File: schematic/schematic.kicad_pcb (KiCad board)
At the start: 2 copper layers, 70 parts, among them J1 Conn_01x04_Socket, J10 Conn_01x06_Pin, J11 Conn_01x06_Pin, J2 Conn_01x04_Socket, J3 Conn_01x04_Socket, J4 Conn_01x04_Socket, J5 Conn_01x03_Pin, J6 Conn_01x03_Pin, J7 Conn_01x03_Pin, J8 Conn_01x03_Pin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

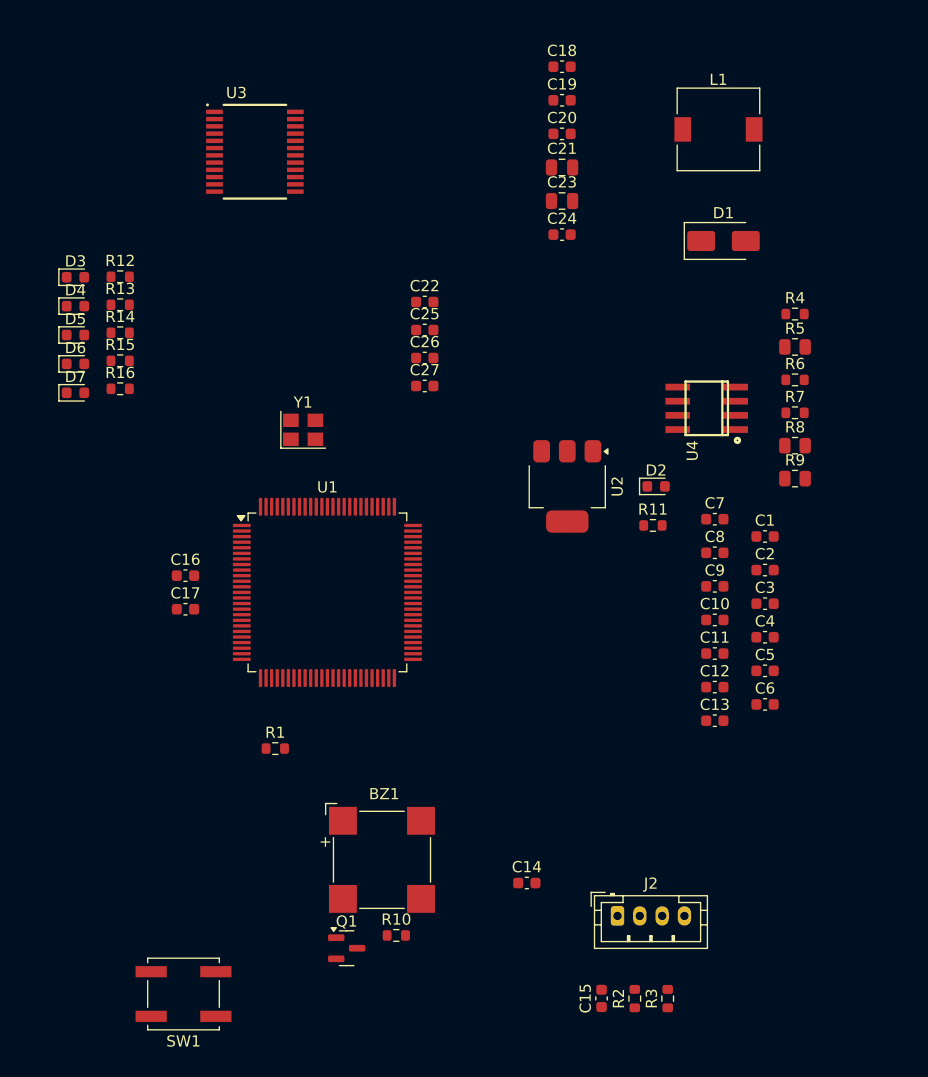
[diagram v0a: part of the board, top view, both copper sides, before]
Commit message: thếu nút nhấn
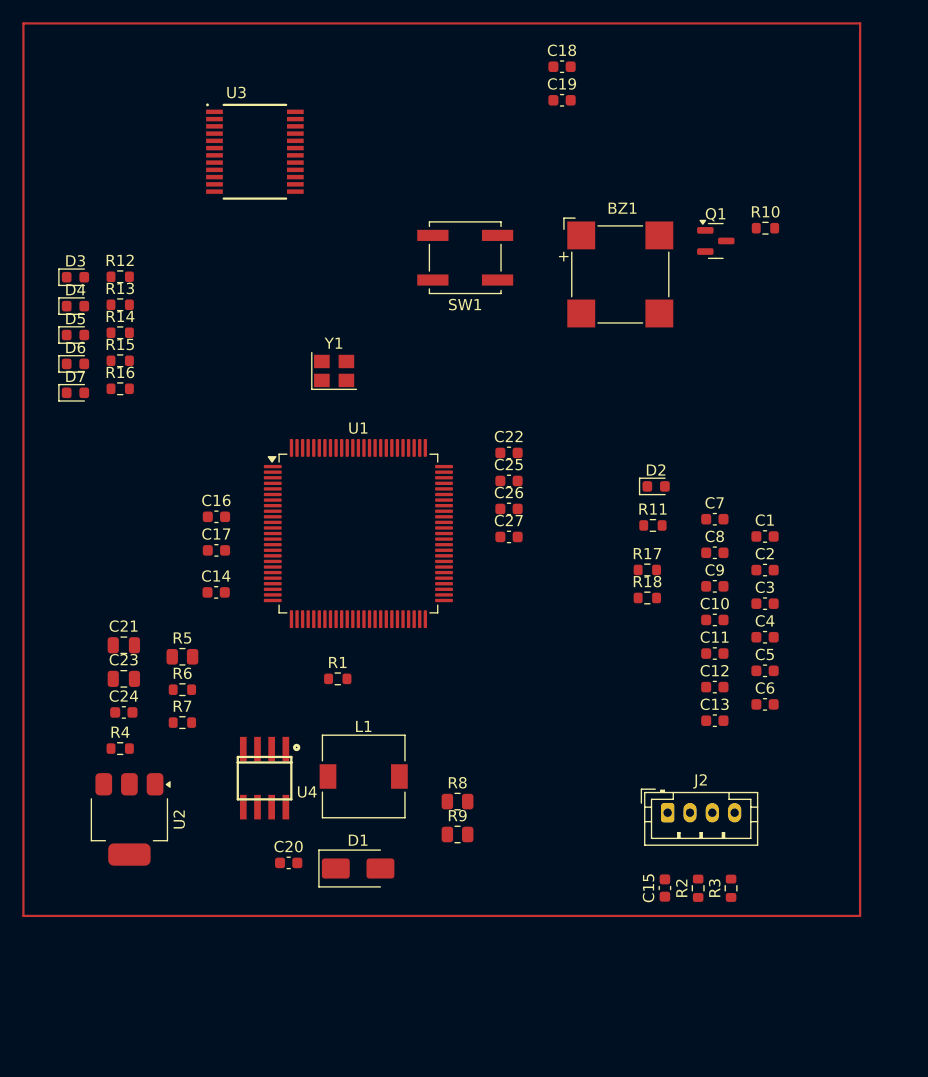
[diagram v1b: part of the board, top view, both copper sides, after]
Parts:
- added R17: 1k, Resistor_SMD:R_0603_1608Metric, F.Cu at (170.7, 97.0)
- added R18: 1k, Resistor_SMD:R_0603_1608Metric, F.Cu at (170.7, 99.5)
- moved R4 71.9 mm to (123.4, 113.0)
- moved Q1 71.5 mm to (176.8, 67.5)
- moved R10 71.5 mm to (181.3, 66.4)
- moved SW1 70.7 mm to (154.3, 69.0)
- moved C20 69.8 mm to (138.5, 123.2)
- moved L1 66.1 mm to (145.2, 115.5)
- moved D1 65.1 mm to (144.8, 123.8)
- moved R5 61.5 mm to (129.0, 104.8)
- moved R6 61.5 mm to (129.0, 107.7)
- moved R7 61.5 mm to (129.0, 110.7)
- moved C21 58.1 mm to (123.8, 103.7)
- moved C23 58.1 mm to (123.8, 106.8)
- moved C24 58.1 mm to (123.8, 109.8)
- moved BZ1 56.7 mm to (168.2, 70.5)
- moved U4 51.7 mm to (136.4, 115.7), turned to 180 degrees
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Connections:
- net /Encoder_A_L renamed /EN_A_L
- net /Encoder_A_R renamed /EN_A_R
- net /Encoder_B_L renamed /EN_B_L
- net /Encoder_B_R renamed /EN_B_R
- net /sensorFF renamed /SS_FF
- net /sensorFL renamed /SS_FL
- net /sensorFR renamed /SS_FR
- net /sensorL renamed /SS_L
- net /sensorR renamed /SS_R

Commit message: no message
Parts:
- added C28: 100nF, Capacitor_SMD:C_0603_1608Metric, F.Cu at (136.2, 86.7)
- added C29: 100nF, Capacitor_SMD:C_0603_1608Metric, F.Cu at (136.2, 89.2)
- added R19: 1k, Resistor_SMD:R_0603_1608Metric, F.Cu at (144.2, 84.1)
- added R20: 1k, Resistor_SMD:R_0603_1608Metric, F.Cu at (144.2, 86.7)
- added SW2: SW_Push, Button_Switch_SMD:SW_Tactile_SPST_NO_Straight_CK_PTS636Sx25SMTRLFS, F.Cu at (151.5, 75.7)
- added SW3: SW_Push, Button_Switch_SMD:SW_Tactile_SPST_NO_Straight_CK_PTS636Sx25SMTRLFS, F.Cu at (151.5, 81.0)
- C12, C13, C26, C27: moved to B.Cu
- R17, R18: value 1k -> 4.7k
- SW1: footprint Button_Switch_SMD:SW_Push_1P1T_NO_CK_KSC6xxJ -> Button_Switch_SMD:SW_Tactile_SPST_NO_Straight_CK_PTS636Sx25SMTRLFS
- moved C19 129.5 mm to (54.3, 125.2), turned to 180 degrees
- moved C13 122.4 mm to (57.4, 83.3), turned to 180 degrees
- moved J7 119.7 mm to (107.2, 89.5)
- moved C12 119.6 mm to (57.9, 93.5), turned to 90 degrees
- moved C4 114.8 mm to (69.0, 78.9)
- moved C18 114.7 mm to (62.5, 107.0), turned to 90 degrees
- moved C6 113.3 mm to (69.0, 93.3)
- moved C5 112.5 mm to (69.1, 97.6)
- moved C2 112.3 mm to (69.0, 91.3)
- moved C1 112.2 mm to (69.0, 95.6)
- moved C3 112.2 mm to (69.1, 99.3)
- moved J6 107.8 mm to (107.2, 79.8)
- moved J1 106.0 mm to (117.2, 70.5)
- moved C11 105.8 mm to (73.2, 82.8)
- moved C10 105.6 mm to (73.2, 80.7)
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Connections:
- U1 pad 82: unconnected-(U1-PD1-Pad82) -> /BUTTON_0
- U1 pad 83: unconnected-(U1-PD2-Pad83) -> /BUTTON_1
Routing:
- net +5V: track 0.00 -> 35.2 mm, vias 0 -> 2
- net +3V3: track 0.00 -> 14.2 mm
- net Net-(U4-FREQ): track 0.00 -> 14.1 mm
- net Net-(U4-BST): track 0.00 -> 13.0 mm, vias 0 -> 2
- net Net-(U4-EN): track 0.00 -> 10.7 mm
- net Net-(U4-FB): track 0.00 -> 7.97 mm
- net Net-(D1-K): track 0.00 -> 6.63 mm
- net Net-(U4-COMP): track 0.00 -> 5.29 mm
- net Net-(C13-Pad1): track 0.00 -> 2.49 mm, vias 0 -> 1
- net Net-(U1-BOOT0): track 0.00 -> 2.12 mm
- net Net-(C12-Pad1): track 0.00 -> 2.12 mm, vias 0 -> 1
- net Net-(C21-Pad2): track 0.00 -> 1.83 mm
- net GND: track 0.00 -> 1.40 mm, vias 0 -> 1
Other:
- board outline added: 65 x 85 mm

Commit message: trc khi xoá ve lai
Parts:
- added J12: Conn_01x02_Socket, Connector_JST:JST_XA_B02B-XASK-1_1x02_P2.50mm_Vertical, F.Cu at (158.7, 134.4)
- C1, C10, C11, C14, C16, C17, C18, C2, C3, C4, C5, C6, C7, C8, C9, J10, J11, J5, J6, R19, R20, Y1: moved to B.Cu
- moved D1 119.0 mm to (165.7, 129.8), turned to 0 degrees
- moved C20 115.4 mm to (159.9, 122.8)
- moved R6 112.4 mm to (154.7, 128.0), turned to 180 degrees
- moved L1 111.0 mm to (165.2, 123.1), turned to 90 degrees
- moved C12 102.5 mm to (160.2, 86.2), turned to -90 degrees
- moved U4 101.6 mm to (156.3, 123.1), turned to 180 degrees
- moved U1 101.5 mm to (154.3, 88.9), turned to 90 degrees
- moved C18 101.3 mm to (162.8, 121.3), turned to -90 degrees
- moved C22 98.3 mm to (162.9, 104.8), turned to -90 degrees
- moved C19 98.1 mm to (152.1, 132.2), turned to 90 degrees
- moved C25 96.9 mm to (161.2, 104.8)
- moved R8 96.1 mm to (150.1, 132.4), turned to -90 degrees
- moved R1 95.0 mm to (144.6, 92.9), turned to 90 degrees
- moved C13 94.0 mm to (151.3, 84.4), turned to -90 degrees
- moved R4 92.9 mm to (152.6, 123.0), turned to 90 degrees
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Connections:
- J10 pad 3: /EN_A_R -> /EN_B_L
- J10 pad 4: /EN_B_R -> /EN_A_L
- J10 pad 5: /M1-L -> /M1-R
- J10 pad 6: /M1-R -> /M1-L
- J11 pad 3: /EN_B_L -> /EN_A_R
- J11 pad 4: /EN_A_L -> /EN_B_R
- J4 pad 1: 5V -> +5V
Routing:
- net +3V3: track 14.2 -> 207.7 mm, vias 0 -> 17
- net +5V: track 35.2 -> 115.3 mm, vias 2 -> 13
- net GND: track 1.40 -> 75.5 mm, vias 1 -> 7
- net /EN_A_L: track 0.00 -> 72.9 mm, vias 0 -> 4
- net /PWMA: track 0.00 -> 36.7 mm, vias 0 -> 2
- net /M1-L: track 0.00 -> 33.4 mm
- net /BIN2: track 0.00 -> 32.9 mm, vias 0 -> 2
- net /NRST: track 0.00 -> 31.4 mm, vias 0 -> 3
- net /BIN1: track 0.00 -> 30.7 mm, vias 0 -> 2
- net /M2-L: track 0.00 -> 30.5 mm, vias 0 -> 4
- net /EN_B_L: track 0.00 -> 27.1 mm
- net 6.5-7.5V: track 0.00 -> 24.2 mm
- net /M1-R: track 0.00 -> 24.0 mm
- net /M2-R: track 0.00 -> 23.9 mm, vias 0 -> 4
- net /AIN1: track 0.00 -> 20.8 mm, vias 0 -> 2
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- added copper zone on F.Cu, net +5V
- added copper zone on B.Cu, net GND
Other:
- outline, holes or cut-outs redrawn

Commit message: 1
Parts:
- added C30: 22uF, Capacitor_SMD:C_0201_0603Metric, F.Cu at (84.3, 147.6)
- added C31: 22uF, Capacitor_SMD:C_0201_0603Metric, F.Cu at (84.3, 149.4)
- added R21: 1.1R, Resistor_SMD:R_0805_2012Metric, F.Cu at (80.9, 148.2)
- added RN1: R_Network05, Resistor_SMD:R_Array_Convex_5x0603, F.Cu at (74.2, 130.3)
- added RN2: R_Pack05, Resistor_SMD:R_Array_Convex_5x0603, F.Cu at (51.5, 140.0)
- added SW4: SW_DIP_x05, Button_Switch_SMD:SW_DIP_SPSTx05_Slide_KingTek_DSHP05TS_W7.62mm_P1.27mm, F.Cu at (59.4, 140.2)
- added U5: AMS1117-5.0, Package_TO_SOT_SMD:SOT-223-3_TabPin2, F.Cu at (83.6, 142.6)
- C14, C16, C17, C18, C26, C27, R19, R20, Y1: moved to F.Cu
- J1, J4: footprint Connector_JST:JST_PH_B4B-PH-K_1x04_P2.00mm_Vertical -> Connector_PinHeader_2.54mm:PinHeader_1x04_P2.54mm_Vertical
- J10, J11: footprint Connector_JST:JST_PH_S6B-PH-K_1x06_P2.00mm_Horizontal -> JST-254:JST 6
- J2: footprint Connector_JST:JST_PH_B4B-PH-K_1x04_P2.00mm_Vertical -> Connector_JST:JST_SH_BM04B-SRSS-TB_1x04-1MP_P1.00mm_Vertical
- J5, J6: footprint Connector_JST:JST_PH_S3B-PH-K_1x03_P2.00mm_Horizontal -> Connector_PinHeader_2.54mm:PinHeader_1x03_P2.54mm_Vertical; moved to F.Cu
- J7: footprint Connector_JST:JST_PH_S3B-PH-K_1x03_P2.00mm_Horizontal -> Connector_PinHeader_2.54mm:PinHeader_1x03_P2.54mm_Vertical
- J8, J9: footprint Connector_JST:JST_PH_B3B-PH-K_1x03_P2.00mm_Vertical -> Connector_PinHeader_2.54mm:PinHeader_1x03_P2.54mm_Vertical
- R1, R2, R3: moved to B.Cu
- moved C24 130.0 mm to (57.0, 83.1), turned to 0 degrees
- moved J4 125.5 mm to (49.9, 119.3)
- moved R18 120.4 mm to (65.0, 88.1), turned to 0 degrees
- moved J12 120.4 mm to (40.5, 111.3), turned to 0 degrees
- moved R17 119.3 mm to (65.0, 85.6), turned to 0 degrees
- moved R11 117.7 mm to (61.0, 93.1), turned to 0 degrees
- moved C28 116.9 mm to (57.0, 93.1)
- moved C29 116.9 mm to (57.0, 95.6)
- moved U4 115.6 mm to (40.7, 119.7), turned to 0 degrees
- moved U2 113.8 mm to (63.8, 119.6), turned to 0 degrees
- moved C18 112.7 mm to (53.0, 95.6), turned to 0 degrees
- moved C20 112.2 mm to (57.0, 78.1), turned to 0 degrees
- moved C19 110.7 mm to (57.0, 75.6), turned to 0 degrees
- moved C22 108.7 mm to (57.0, 80.6), turned to 0 degrees
- moved C23 107.4 mm to (69.2, 94.6), turned to 0 degrees
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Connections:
- D3 pad 1: GND -> Net-(D3-K)
- D3 pad 2: Net-(D3-A) -> /LED_FL
- D4 pad 1: GND -> Net-(D4-K)
- D4 pad 2: Net-(D4-A) -> /LED_L
- D5 pad 1: GND -> Net-(D5-K)
- D5 pad 2: Net-(D5-A) -> /LED_FF
- D6 pad 1: GND -> Net-(D6-K)
- D6 pad 2: Net-(D6-A) -> /LED_FR
- D7 pad 1: GND -> Net-(D7-K)
- D7 pad 2: Net-(D7-A) -> /LED_R
- J10 pad 5: /M1-R -> /M2-L
- J10 pad 6: /M1-L -> /M2-R
- J11 pad 5: /M2-L -> /M1-R
- J11 pad 6: /M2-R -> /M1-L
- U1 pad 1: unconnected-(U1-PE2-Pad1) -> /BIT_SW_4
- U1 pad 2: unconnected-(U1-PE3-Pad2) -> /BIT_SW_3
- U1 pad 24: unconnected-(U1-PA2-Pad24) -> /BUTTON_0
- U1 pad 25: unconnected-(U1-PA3-Pad25) -> /BUTTON_1
- U1 pad 29: /EN_A_L -> unconnected-(U1-PA5-Pad29)
- U1 pad 3: unconnected-(U1-PE4-Pad3) -> /BIT_SW_2
- U1 pad 39: /PWMA -> unconnected-(U1-PE9-Pad39)
- U1 pad 4: unconnected-(U1-PE5-Pad4) -> /BIT_SW_1
- U1 pad 41: /PWMB -> unconnected-(U1-PE11-Pad41)
- U1 pad 5: unconnected-(U1-PE6-Pad5) -> /BIT_SW_0
- U1 pad 53: /UART1_TX -> unconnected-(U1-PB14-Pad53)
- U1 pad 54: /UART1_RX -> unconnected-(U1-PB15-Pad54)
- U1 pad 61: unconnected-(U1-PD14-Pad61) -> /BUZZ
- U1 pad 62: unconnected-(U1-PD15-Pad62) -> /LED_L
- U1 pad 63: /LED_L -> /LED_FL
- U1 pad 64: /LED_R -> /LED_FF
- U1 pad 65: /LED_FL -> /LED_FR
- U1 pad 66: /LED_FR -> /LED_R
- U1 pad 67: /LED_FF -> /PWMA
- U1 pad 68: /BUZZ -> /PWMB
- U1 pad 77: unconnected-(U1-PA15-Pad77) -> /EN_A_L
- U1 pad 82: /BUTTON_0 -> unconnected-(U1-PD1-Pad82)
- U1 pad 83: /BUTTON_1 -> unconnected-(U1-PD2-Pad83)
- U1 pad 87: /BIN1 -> /BIN2
- U1 pad 88: /BIN2 -> /BIN1
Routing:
- net +3V3: track 207.7 -> 35.2 mm, vias 17 -> 8
- net +5V: track 115.3 -> 0.00 mm, vias 13 -> 0
- net GND: track 75.5 -> 0.00 mm, vias 7 -> 0
- net /EN_A_L: track 72.9 -> 0.00 mm, vias 4 -> 0
- net /PWMA: track 36.7 -> 0.00 mm, vias 2 -> 0
- net /M1-L: track 33.4 -> 0.00 mm
- net /BIN2: track 32.9 -> 0.00 mm, vias 2 -> 0
- net /NRST: track 31.4 -> 0.00 mm, vias 3 -> 0
- net /BIN1: track 30.7 -> 0.00 mm, vias 2 -> 0
- net /M2-L: track 30.5 -> 0.00 mm, vias 4 -> 0
- net /EN_B_L: track 27.1 -> 0.00 mm
- net 6.5-7.5V: track 24.2 -> 0.00 mm
- net /M1-R: track 24.0 -> 0.00 mm
- net /M2-R: track 23.9 -> 0.00 mm, vias 4 -> 0
- net Net-(U4-EN): track 21.7 -> 0.00 mm, vias 2 -> 0
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- removed copper zone on F.Cu, net +5V
- removed copper zone on B.Cu, net GND
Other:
- outline, holes or cut-outs redrawn

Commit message: gần hoàn thiện pcb
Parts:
- removed D6, D7: LED, LED_SMD:LED_0603_1608Metric
- removed J3: Conn_01x04_Socket, Connector_JST:JST_PH_B4B-PH-K_1x04_P2.00mm_Vertical
- removed J6, J7, J8, J9: Conn_01x03_Pin, Connector_PinHeader_2.54mm:PinHeader_1x03_P2.54mm_Vertical
- removed R12, R13, R14, R15, R16: 1K, Resistor_SMD:R_0603_1608Metric
- added C32: 10uF, Capacitor_Tantalum_SMD:CP_EIA-3216-10_Kemet-I, F.Cu at (186.6, 117.2)
- added D8: LED, LED_SMD:LED_0603_1608Metric, F.Cu at (173.7, 57.8)
- added D9: LED, LED_SMD:LED_0603_1608Metric, F.Cu at (176.3, 57.8)
- C14, C15, C23, C24, C27, C28, C29, C30, R11, R19, R20, RN2, U3: moved to B.Cu
- C25: footprint Capacitor_SMD:C_0603_1608Metric -> Capacitor_Tantalum_SMD:CP_EIA-3216-10_Kemet-I
- C26: footprint Capacitor_SMD:C_0603_1608Metric -> Capacitor_Tantalum_SMD:CP_EIA-3216-10_Kemet-I; moved to B.Cu
- J1, J4: footprint Connector_PinHeader_2.54mm:PinHeader_1x04_P2.54mm_Vertical -> JST-254:JST 4
- J10, J11: footprint JST-254:JST 6 -> Connector_JST:JST_SH_BM06B-SRSS-TB_1x06-1MP_P1.00mm_Vertical
- J2: footprint Connector_JST:JST_SH_BM04B-SRSS-TB_1x04-1MP_P1.00mm_Vertical -> JST-254:JST 4
- J5: value Conn_01x03_Pin -> Conn_01x07_Pin; footprint Connector_PinHeader_2.54mm:PinHeader_1x03_P2.54mm_Vertical -> Connector_PinHeader_2.54mm:PinHeader_1x07_P2.54mm_Vertical; moved to B.Cu
- moved RN2 151.1 mm to (195.2, 93.3)
- moved C24 148.4 mm to (203.9, 104.2)
- moved SW4 143.7 mm to (195.2, 93.3), turned to 180 degrees
- moved R11 143.2 mm to (203.9, 102.3), turned to 180 degrees
- moved U2 140.9 mm to (203.9, 104.0)
- moved C16 139.8 mm to (192.4, 81.6), turned to 180 degrees
- moved C17 139.7 mm to (192.5, 86.8), turned to 180 degrees
- moved C14 137.8 mm to (184.8, 125.6)
- moved J1 135.4 mm to (185.3, 100.4), turned to 180 degrees
- moved C23 135.4 mm to (204.1, 106.3)
- moved J5 133.1 mm to (172.8, 68.4), turned to -90 degrees
- moved C18 131.7 mm to (182.8, 117.6), turned to 90 degrees
- moved C22 131.4 mm to (185.2, 109.0)
- moved RN1 131.4 mm to (179.1, 51.2), turned to -90 degrees
- moved C25 130.4 mm to (185.6, 107.2)
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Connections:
- J10 pad 5: /M2-L -> /M2-R
- J10 pad 6: /M2-R -> /M2-L
- J11 pad 5: /M1-R -> /M1-L
- J11 pad 6: /M1-L -> /M1-R
- J5 pad 1: GND -> /SS_L
- J5 pad 2: /SS_FF -> /SS_R
- J5 pad 3: +5V -> /SS_FL
- R21 pad 1: +7.5V -> 6.5-7.5V
- U1 pad 1: /BIT_SW_4 -> /BIT_SW_0
- U1 pad 2: /BIT_SW_3 -> /BIT_SW_1
- U1 pad 4: /BIT_SW_1 -> /BIT_SW_3
- U1 pad 5: /BIT_SW_0 -> /BIT_SW_4
- U1 pad 62: /LED_L -> /LED_FL
- U1 pad 63: /LED_FL -> /LED_L
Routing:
- net +5V: track 0.00 -> 186.0 mm, vias 0 -> 20
- net +3V3: track 35.2 -> 214.7 mm, vias 8 -> 18
- net /BUTTON_0: track 0.00 -> 78.6 mm, vias 0 -> 1
- net /NRST: track 0.00 -> 52.4 mm, vias 0 -> 2
- net 6.5-7.5V: track 0.00 -> 52.0 mm
- net /BUTTON_1: track 0.00 -> 48.5 mm, vias 0 -> 2
- net /LED_FL: track 0.00 -> 44.0 mm
- net /LED_FR: track 0.00 -> 43.1 mm
- net /LED_L: track 0.00 -> 43.0 mm
- net /LED_FF: track 0.00 -> 42.1 mm
- net /LED_R: track 0.00 -> 40.0 mm
- net /PWMA: track 0.00 -> 33.5 mm, vias 0 -> 3
- net /EN_B_L: track 0.00 -> 31.6 mm, vias 0 -> 1
- net /I2C2_SCL: track 0.00 -> 31.4 mm, vias 0 -> 1
- net Net-(U4-FB): track 0.00 -> 31.1 mm
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- added copper zone on F.Cu, net +3V3
- added copper zone on B.Cu, net +5V
- added copper zone on F.Cu, net +5V
- added copper zone on B.Cu, net /M1-L
- added copper zone on B.Cu, net /M1-R
- added copper zone on B.Cu, net /M2-L
- added copper zone on B.Cu, net /M2-R
- added copper zone on F.Cu, net 6.5-7.5V
- added copper zone on B.Cu, net GND
- added copper zone on F.Cu, net GND

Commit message: cho doi xi va
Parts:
- C16, C17, Y1: moved to B.Cu
- C23: value 10uF -> 22uF; footprint Capacitor_SMD:C_0805_2012Metric -> Capacitor_Tantalum_SMD:CP_EIA-3216-10_Kemet-I
- C24: value 10uF -> 22uF; footprint Capacitor_SMD:C_0603_1608Metric -> Capacitor_Tantalum_SMD:CP_EIA-3216-10_Kemet-I
- C30: footprint Capacitor_SMD:C_0201_0603Metric -> Capacitor_Tantalum_SMD:CP_EIA-3216-10_Kemet-I
- C31: footprint Capacitor_SMD:C_0201_0603Metric -> Capacitor_Tantalum_SMD:CP_EIA-3216-10_Kemet-I; moved to B.Cu
- moved C30 2.80 mm to (204.6, 113.0), turned to 0 degrees
- moved C31 2.49 mm to (205.5, 117.7)
- moved RN1 2.16 mm to (178.9, 53.4)
- moved C24 1.41 mm to (205.3, 104.0)
- moved C23 1.20 mm to (205.3, 106.2)
- moved R11 0.60 mm to (204.3, 101.9)
- moved C17 0.10 mm to (192.4, 86.8), turned to 0 degrees
- turned C16 to 0 degrees
- turned Y1 to 0 degrees
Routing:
- net +3V3: track 214.7 -> 254.1 mm
- net /BUTTON_1: track 48.5 -> 87.8 mm
- net /NRST: track 52.4 -> 78.2 mm
- net /BUTTON_0: track 78.6 -> 95.7 mm, vias 1 -> 3
- net +5V: track 186.0 -> 189.3 mm, vias 20 -> 21
- net Net-(U5-VI): track 5.96 -> 8.87 mm, vias 0 -> 1
- net Net-(D3-K): track 12.3 -> 9.42 mm, vias 0 -> 2
- net Net-(U4-EN): track 12.9 -> 15.5 mm
- net Net-(D9-K): track 5.73 -> 3.24 mm
- net Net-(D5-K): track 6.89 -> 4.82 mm
- net Net-(D8-K): track 8.34 -> 6.34 mm
- net Net-(D4-K): track 7.36 -> 5.39 mm
- net GND: track 15.9 -> 17.6 mm, vias 7 -> 53
- net /PH0: track 8.73 -> 10.5 mm, vias 0 -> 1
- net /PH1: track 12.2 -> 12.9 mm, vias 2 -> 1
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
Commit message: khá ổn chờ chốt
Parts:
- removed BZ1: Buzzer, Buzzer_Beeper:MagneticBuzzer_CUI_CMT-8504-100-SMT
- removed RN1: R_Network05, Resistor_SMD:R_Array_Convex_5x0603
- added G***: LOGO, LOGO, F.Cu at (199.5, 63.9)
- added LS1: CMT-8530S-SMT, Buzzer_Beeper:CUI_CMT-8530S-SMT, F.Cu at (157.0, 65.7)
- added RN3: R_Pack05, Resistor_SMD:R_Array_Convex_5x0603, F.Cu at (178.9, 53.0)
- C22, C25: moved to B.Cu
- PIN: renamed from J12; footprint Connector_JST:JST_XA_B02B-XASK-1_1x02_P2.50mm_Vertical -> Connector_PinHeader_2.54mm:jst; moved to B.Cu
- moved C25 8.47 mm to (177.2, 105.6), turned to 180 degrees
- moved C22 7.88 mm to (177.5, 107.5), turned to 180 degrees
- moved D9 4.72 mm to (188.8, 57.8)
- moved R2 4.05 mm to (157.7, 91.9)
- moved R3 4.05 mm to (160.2, 92.0)
- moved C15 4.05 mm to (152.5, 91.9)
- moved J2 4.05 mm to (162.8, 92.5)
- moved C26 3.85 mm to (171.3, 117.1)
- moved R18 3.46 mm to (157.7, 78.8), turned to -90 degrees
- moved D8 3.23 mm to (170.5, 57.8)
- moved D4 2.77 mm to (184.2, 57.8)
- moved D3 2.14 mm to (174.2, 57.8)
- moved PIN 1.72 mm to (159.9, 125.0), turned to 180 degrees
- moved C18 1.67 mm to (184.5, 117.6)
- moved R4 1.53 mm to (182.9, 117.6)
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- renumbered D9 to D3, D3 to D9
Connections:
- D3 pad 2: /LED_FR -> /LED_FL
- D4 pad 2: /LED_L -> /LED_FR
- D8 pad 2: /LED_R -> /LED_L
- D9 pad 2: /LED_FL -> /LED_R
- J1 pad 2: /UART3_RX -> /UART3_TX
- J1 pad 3: /UART3_TX -> /UART3_RX
- J10 pad 1: +5V -> +3V3
- J11 pad 1: +5V -> +3V3
- J11 pad 3: /EN_A_R -> /EN_B_R
- J11 pad 4: /EN_B_R -> /EN_A_R
- J4 pad 1: +5V -> +3V3
- U1 pad 62: /LED_FL -> /LED_R
- U1 pad 63: /LED_L -> /LED_FR
- U1 pad 65: /LED_FR -> /LED_FL
- U1 pad 66: /LED_R -> /LED_L
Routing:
- net +5V: track 189.3 -> 109.5 mm, vias 21 -> 18
- net /UART3_TX: track 21.9 -> 40.8 mm
- net Net-(D1-K): track 26.3 -> 9.29 mm
- net /LED_R: track 40.0 -> 56.6 mm
- net /UART3_RX: track 23.9 -> 35.7 mm
- net /LED_FR: track 43.1 -> 53.8 mm
- net GND: track 17.6 -> 7.75 mm, vias 53 -> 80
- net /BIN1: track 16.7 -> 25.3 mm
- net /BIN2: track 17.4 -> 25.3 mm
- net /LED_FF: track 42.1 -> 49.6 mm
- net /PWMB: track 25.9 -> 32.7 mm
- net Net-(D3-K): track 3.24 -> 6.69 mm
- net Net-(D8-K): track 6.34 -> 9.63 mm
- net /I2C2_SCL: track 31.4 -> 28.5 mm
- net /LED_FL: track 44.0 -> 46.5 mm
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- added copper zone on F.Cu, net Net-(D1-K)
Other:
- outline, holes or cut-outs redrawn
- board text added: "3V3"
- board text added: "3v3"
- board text added: "5V"
- board text added: "5v"
- board text added: "CLK"
- board text added: "DIO"
- board text added: "FF"
- board text added: "FL"
- board text added: "FR"
- board text added: "GND"
- board text added: "L"
- board text added: "MPU"
- board text added: "R"
- board text added: "RX"
- board text added: "SCL"
- board text added: "SDA"
- board text added: "SENSOR"
- board text added: "TX"
